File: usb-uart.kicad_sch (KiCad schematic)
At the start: 9 parts, among them J2 USB_C_Receptacle_USB2.0

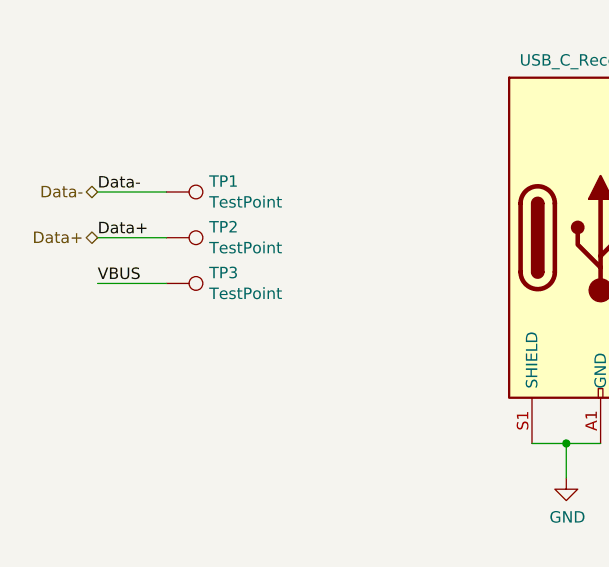
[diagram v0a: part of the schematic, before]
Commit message: changed usb port footprint to the combined SMD/THT one
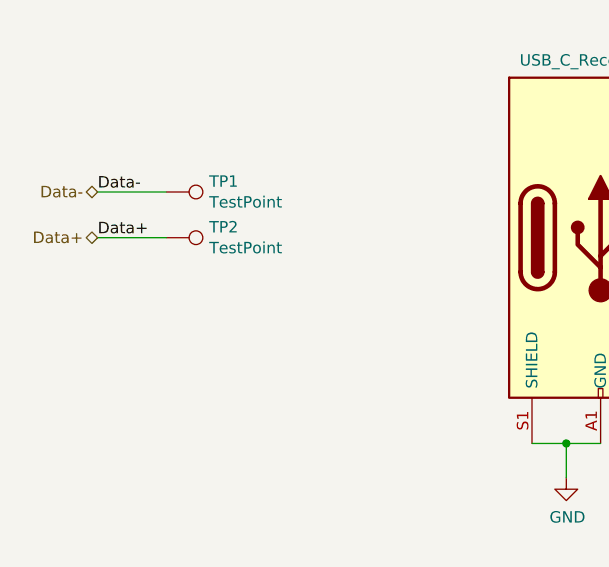
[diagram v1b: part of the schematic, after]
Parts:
- removed TP3: TestPoint, TestPoint:TestPoint_Pad_D1.0mm, symbol Connector:TestPoint
- J2: footprint Connector_USB:USB_C_Receptacle_GCT_USB4085 -> Connector_USB:USB_C_Receptacle_Palconn_UTC16-G
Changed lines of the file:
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@@
-    (stroke (width 0) (type default) (color 0 0 0 0))
-  )
-  (wire (pts (xy 44.45 109.22) (xy 52.07 109.22))
     (stroke (width 0) (type default) (color 0 0 0 0))
   )
@@
   )
   (label "Data-" (at 116.84 102.87 0)
-    (effects (font (size 1.27 1.27)) (justify left bottom))
-  )
-  (label "VBUS" (at 44.45 109.22 0)
     (effects (font (size 1.27 1.27)) (justify left bottom))
   )
@@
     (property "Reference" "J2" (id 0) (at 103.0478 82.1182 0))
     (property "Value" "USB_C_Receptacle_USB2.0" (id 1) (at 103.0478 84.4296 0))
-    (property "Footprint" "Connector_USB:USB_C_Receptacle_GCT_USB4085" (id 2) (at 104.14 104.14 0)
+    (property "Footprint" "Connector_USB:USB_C_Receptacle_Palconn_UTC16-G" (id 2) (at 104.14 104.14 0)
       (effects (font (size 1.27 1.27)) hide)
     )
@@
       (effects (font (size 1.27 1.27)) hide)
     )
-    (pin "1")
-  )
-  (symbol (lib_id "Connector:TestPoint") (at 52.07 109.22 270) (unit 1)
-    (in_bom yes) (on_board yes)
-    (property "Reference" "TP3" (id 0) (at 56.8452 108.0516 90)
-      (effects (font (size 1.27 1.27)) (justify left))
-    )
-    (property "Value" "TestPoint" (id 1) (at 56.8452 110.363 90)
-      (effects (font (size 1.27 1.27)) (justify left))
-    )
-    (property "Footprint" "TestPoint:TestPoint_Pad_D1.0mm" (id 2) (at 52.07 114.3 0)
-      (effects (font (size 1.27 1.27)) hide)
-    )
-    (property "Datasheet" "~" (id 3) (at 52.07 114.3 0)
-      (effects (font (size 1.27 1.27)) hide)
-    )

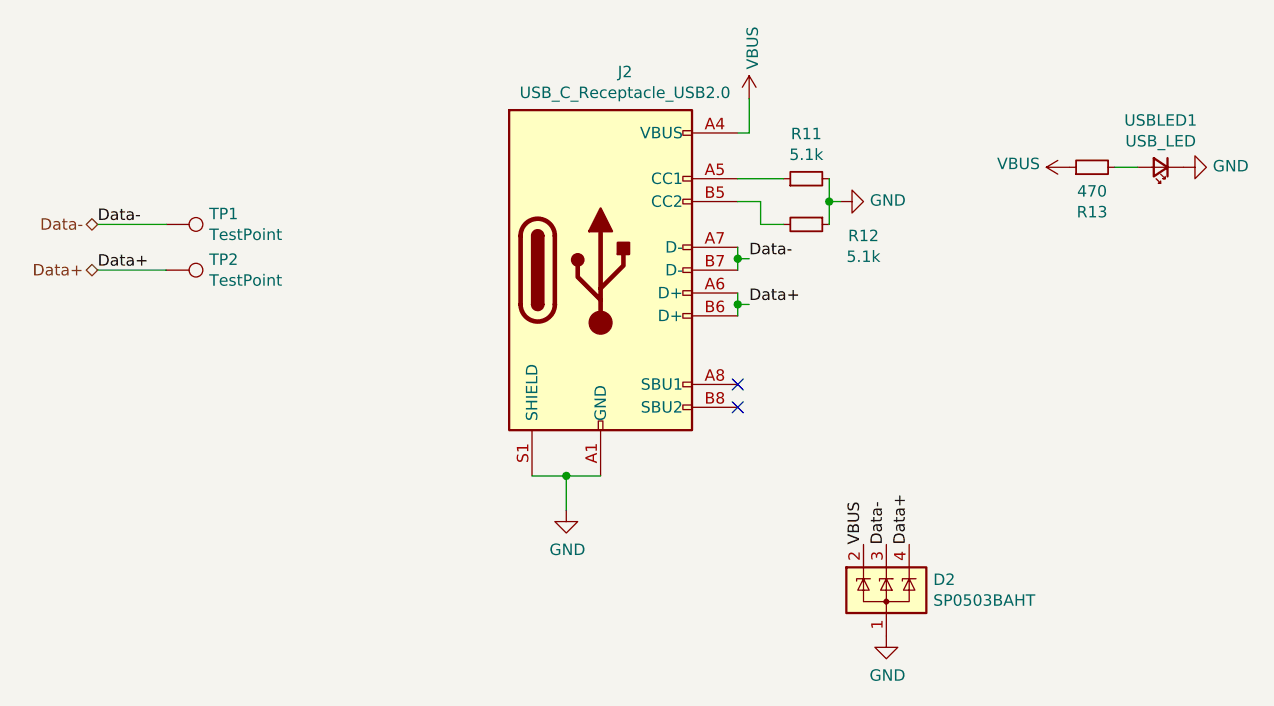
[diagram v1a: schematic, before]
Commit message: updated some schematic values
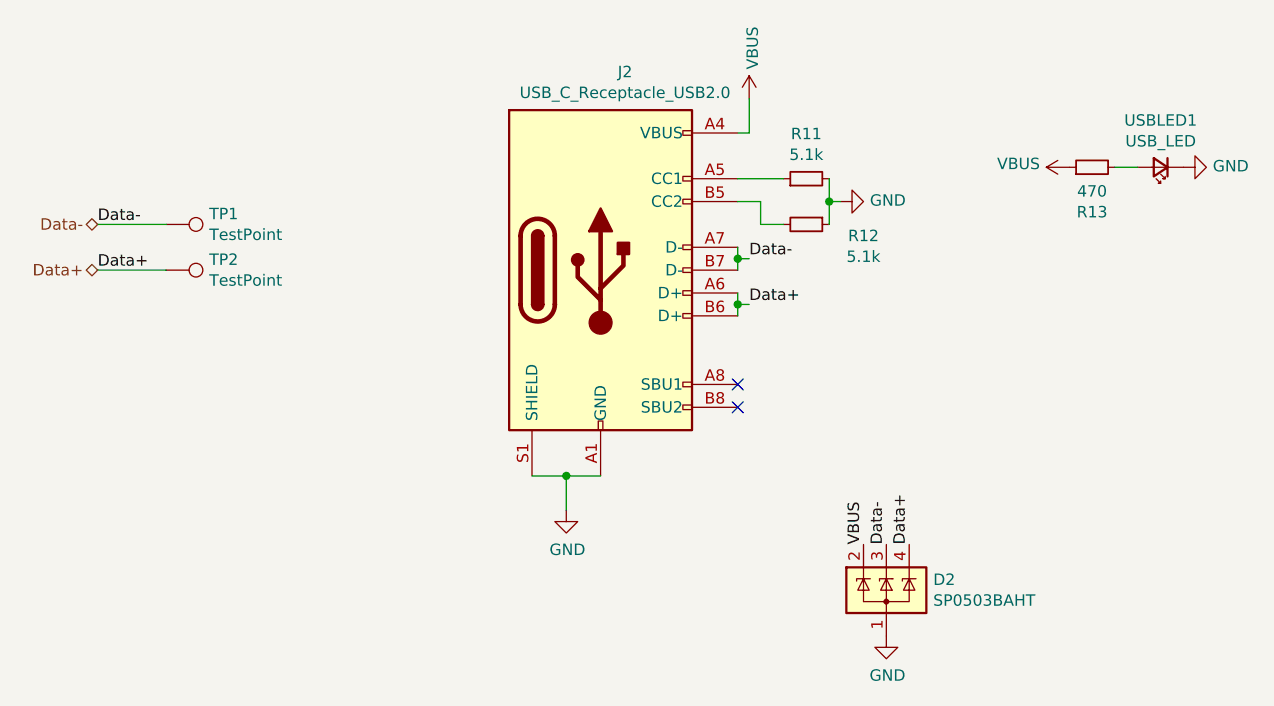
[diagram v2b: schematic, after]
